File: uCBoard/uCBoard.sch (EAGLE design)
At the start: 20 parts, among them X1 22-23-2041

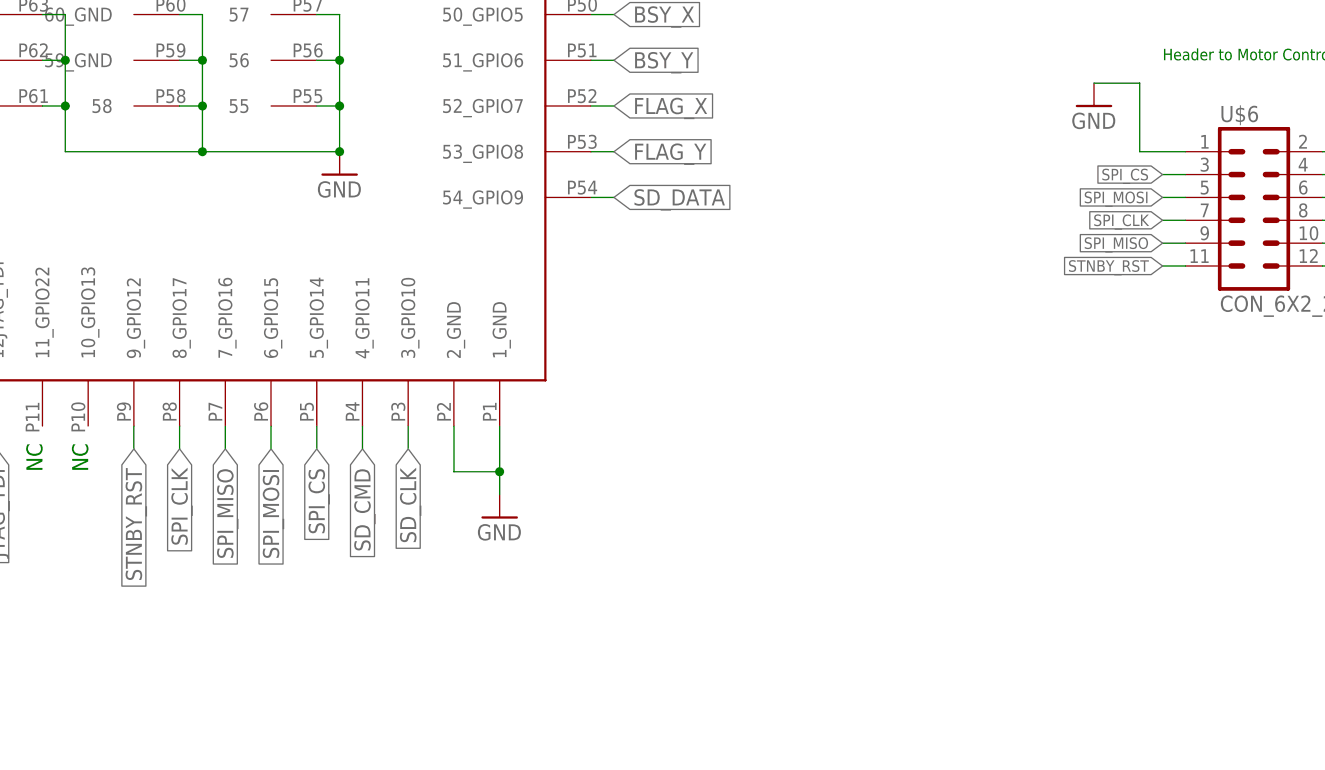
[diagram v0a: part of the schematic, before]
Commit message: Fixing labeling on the uC board so that SPI is correct
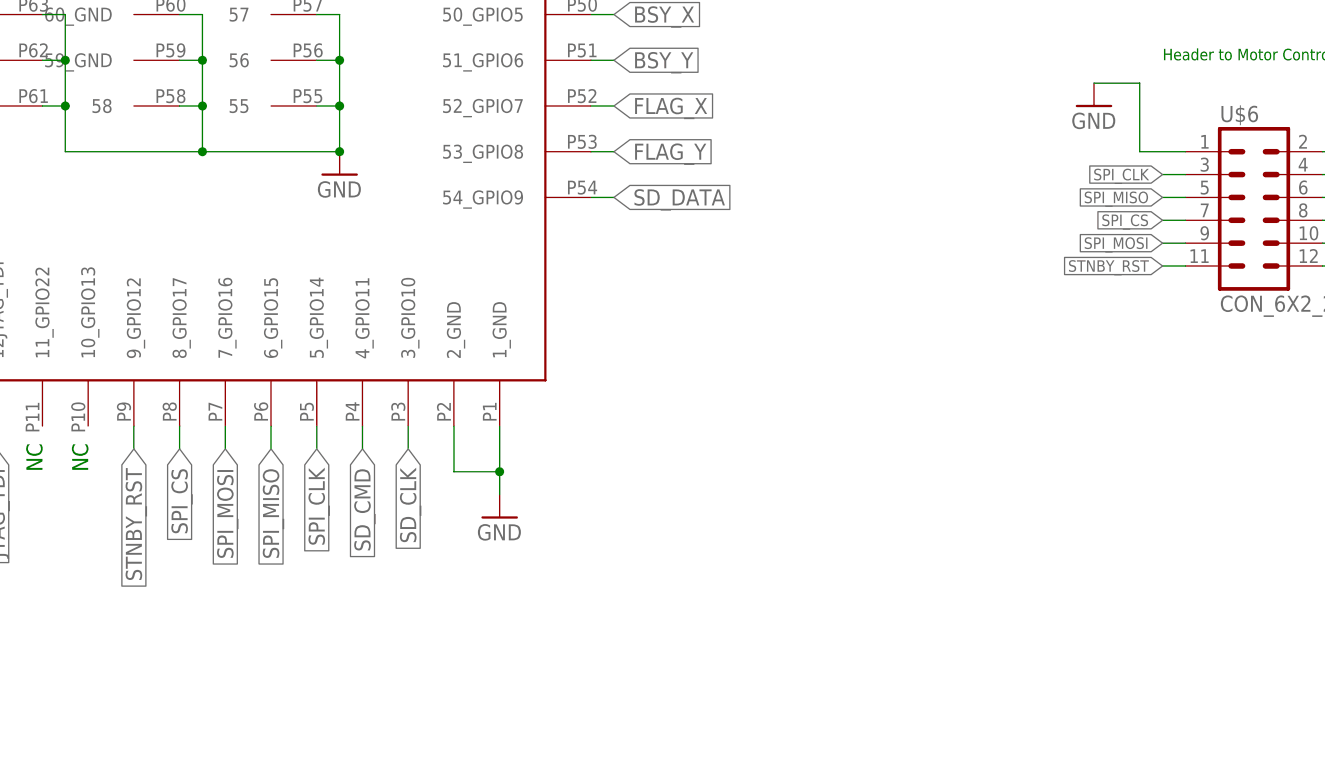
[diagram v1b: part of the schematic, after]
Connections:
- net SPI_CLK: now also U$1.5_GPIO14, U$6.3; no longer U$1.8_GPIO17, U$6.7
- net SPI_CS: now also U$1.8_GPIO17, U$6.7; no longer U$1.5_GPIO14, U$6.3
- net SPI_MISO: now also U$1.6_GPIO15, U$6.5; no longer U$1.7_GPIO16, U$6.9
- net SPI_MOSI: now also U$1.7_GPIO16, U$6.9; no longer U$1.6_GPIO15, U$6.5
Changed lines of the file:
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@@
 </segment>
 </net>
-<net name="SPI_CS" class="0">
+<net name="SPI_CLK" class="0">
 <segment>
 <pinref part="U$6" gate="G$1" pin="3"/>
@@
 </segment>
 </net>
-<net name="SPI_MISO" class="0">
+<net name="SPI_MOSI" class="0">
 <segment>
 <pinref part="U$6" gate="G$1" pin="9"/>
@@
 </segment>
 </net>
-<net name="SPI_CLK" class="0">
+<net name="SPI_CS" class="0">
 <segment>
 <pinref part="U$6" gate="G$1" pin="7"/>
@@
 <wire x1="226.06" y1="132.08" x2="226.06" y2="129.54" width="0.1524" layer="91"/>
 <label x="226.06" y="129.54" size="1.778" layer="95" rot="R270" xref="yes"/>
-</segment>
-</net>
-<net name="SPI_MOSI" class="0">
-<segment>
-<pinref part="U$6" gate="G$1" pin="5"/>
-<wire x1="337.82" y1="157.48" x2="335.28" y2="157.48" width="0.1524" layer="91"/>
-<label x="335.28" y="157.48" size="1.27" layer="95" rot="R180" xref="yes"/>
-</segment>
-<segment>
-<pinref part="U$1" gate="G$1" pin="6_GPIO15"/>
-<wire x1="236.22" y1="132.08" x2="236.22" y2="129.54" width="0.1524" layer="91"/>
-<label x="236.22" y="129.54" size="1.778" layer="95" rot="R270" xref="yes"/>
 </segment>
 </net>
@@
 </segment>
 </net>
+<net name="SPI_MISO" class="0">
+<segment>
+<pinref part="U$1" gate="G$1" pin="6_GPIO15"/>
+<wire x1="236.22" y1="132.08" x2="236.22" y2="129.54" width="0.1524" layer="91"/>
+<label x="236.22" y="129.54" size="1.778" layer="95" rot="R270" xref="yes"/>
+</segment>
+<segment>
+<pinref part="U$6" gate="G$1" pin="5"/>
+<wire x1="337.82" y1="157.48" x2="335.28" y2="157.48" width="0.1524" layer="91"/>
+<label x="335.28" y="157.48" size="1.27" layer="95" rot="R180" xref="yes"/>
+</segment>
+</net>
